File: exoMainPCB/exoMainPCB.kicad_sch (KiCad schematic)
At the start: 1 part

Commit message: centralized schematic sheets into one sheet
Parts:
- added C1, C11, C12, C17, C2, C3, C35, C4: 22 pF, symbol Device:C
- added C10, C27, C30: 0.1 uF, symbol Device:C
- added C13, C14, C8, C9: 100uF, symbol Device:C
- added C15, C16: 10 uF, symbol Device:C
- added C28, C29, C31, C32: 28 pF, symbol Device:C
- added C33, C34, C5, C6: 104, symbol Device:C
- added C7: 100n, symbol Device:C
- added D1, D15, D16, D17, D18, D19, D2, D3: PESD5V0L4UF, Package_TO_SOT_SMD:SOT-886, symbol Power_Protection:PESD5V0L4UF
- added D12, D13, D14: LED, symbol Device:LED
- added J1: Conn_02x06_Odd_Even, symbol Connector_Generic:Conn_02x06_Odd_Even
- added J10, J6: Conn_01x03_Pin, symbol Connector:Conn_01x03_Pin
- added J11, J12, J13, J3: USB_A, symbol Connector:USB_A
- added J2: HDMI_A, symbol Connector:HDMI_A
- added JP1, JP2, JP7, JP8: SolderJumper_2_Open, symbol Jumper:SolderJumper_2_Open
- added Q3, Q4: S8550, Package_TO_SOT_THT:TO-92_Inline, symbol Transistor_BJT:S8550
- added R1, R2: 2.2 kOhm, symbol Device:R_US
- added R10, R8: 2.2k, symbol Device:R_US
- added R11, R4, R5: 10k, symbol Device:R_US
- added R13, R15, R16: R_US, symbol Device:R_US
- added R17, R3, R9: 10 kOhm, symbol Device:R_US
- added R22, R24: 12 kOhm, symbol Device:R_US
- added R23, R25: 17 kOhm, symbol Device:R_US
- added R26, R27: 120, symbol Device:R_US
- added R6, R7: 1k, symbol Device:R_US
- added SW3, SW4: SW_SPDT, symbol Switch:SW_SPDT
- added U1, U2: MCP2515-I/ST, SOP65P640X120-20N, symbol MCP2515-IST:MCP2515-I_ST
- added U12, U13: HX711, Package_SO:SOP-16_3.9x9.9mm_P1.27mm, symbol Analog_ADC:HX711
- added U14: SI8642ED-B-IS, SOIC127P1030X265-16N, symbol SI8642ED-B-IS:Si8642ED-B-IS
- added U15, U16: SN65HVD230D, SOIC127P600X175-8N, symbol SN65HVD230:SN65HVD230D
- added U17, U18: SM24CANB-02HTG, SM24CANB02HTG, symbol SM24CANB:SM24CANB-02HTG
- added U3: BNO085, BNO085:IC_BNO085, symbol BNO085:BNO085
- added U4: SL2.1A, my_lib:SOP-16_L10.0-W3.9-P1.27-LS6.0-BL, symbol SL2.1A:SL2.1A
- added Y1, Y2: 16 MHz, symbol Device:Crystal
- added Y3: 12 MHz, symbol Device:Crystal
- added Y4: 32.768 kHz, symbol Device:Crystal
- added Y7, Y8: 18.432 MHz, symbol Device:Crystal
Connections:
- new net: C10.1, U3.9 (CAP)
- new net: R27.1, SW4.2 (B)
- new net: J10.3 (Pin_3), R27.2, U16.7 (CANH), U18.1
- new net: R5.2, U2.19 (~{RESET})
- new net: R5.1, U2.20 (VDD)
- new net: C3.2, U2.8 (OSC2), Y2.2
- new net: C4.2, U2.9 (OSC1), Y2.1
- new net: D13.2 (A), R15.1
- new net: C15.2, U4.14 (VDD18)
- new net: C29.1, U12.14 (XI), Y7.1
- new net: C28.2, U12.13 (XO), Y7.2
- new net: C32.1, U13.14 (XI), Y8.1
- new net: C31.2, U13.13 (XO), Y8.2
- new net: R26.1, SW3.2 (B)
- new net: J6.3 (Pin_3), R26.2, U15.7 (CANH), U17.1
- new net: C35.2, U4.15 (XOUT), Y3.2
- new net: D14.2 (A), R16.1
- new net: J3.2 (D-), U4.1 (DM4)
- new net: C16.2, U4.13 (VDD33)
- new net: C17.2, U4.16 (XIN), Y3.1
- new net: J3.3 (D+), U4.2 (DP4)
- new net: J11.2 (D-), U4.3 (DM3)
- new net: J11.3 (D+), U4.4 (DP3)
- new net: J12.2 (D-), U4.5 (DM2)
- new net: J12.3 (D+), U4.6 (DP2)
- new net: J13.2 (D-), U4.7 (DM1)
- new net: J13.3 (D+), U4.8 (DP1)
- new net: C34.1, U16.3 (VCC)
- new net: J6.2 (Pin_2), SW3.1 (A), U15.6 (CANL), U17.2
- new net: R7.2, U16.8 (RS)
- new net: J10.2 (Pin_2), SW4.1 (A), U16.6 (CANL), U18.2
- new net: R22.2, R23.1, U12.4 (VFB)
- new net: C5.2, U14.1 (VDD1)
- new net: C6.1, U14.16 (VDD2)
- new net: Q4.2 (B), U13.2 (BASE)
- new net: R4.1, U1.20 (VDD)
- new net: R4.2, U1.19 (~{RESET})
- new net: D12.2 (A), R13.1
- new net: C1.2, U1.8 (OSC2), Y1.2
- new net: C2.2, U1.9 (OSC1), Y1.1
- new net: Q3.2 (B), U12.2 (BASE)
- new net: C27.1, U12.6 (VBG)
- new net: C33.1, U15.3 (VCC)
- new net: C11.1, U3.26 (XOUT32/CLKSEL1), Y4.1
- new net: R6.2, U15.8 (RS)
- new net: R24.2, R25.1, U13.4 (VFB)
- new net: U3.1 (RESV_NC), U3.12 (RESV_NC), U3.13 (RESV_NC), U3.21 (RESV_NC), U3.22 (RESV_NC), U3.23 (RESV_NC), U3.24 (RESV_NC), U3.7 (RESV_NC), U3.8 (RESV_NC)
- new net: C12.1, U3.27 (XIN32), Y4.2
- new net: C30.1, U13.6 (VBG)
- new net +24V: J1.11 (Pin_11), J1.7 (Pin_7), J1.8 (Pin_8)
- new net +3V3: Q3.1 (E), Q4.1 (E), R1.1, R10.2, R11.2, R17.1, R2.1, R3.1, R8.2, R9.2, U12.1 (VSUP), U12.15 (RATE), U12.16 (DVDD), U13.1 (VSUP), U13.15 (RATE), U13.16 (DVDD), U3.28 (VDDIO), U3.3 (VDD)
- new net +5V: C13.1, C14.1, C7.2, C8.1, C9.1, J1.1 (Pin_1), J1.2 (Pin_2), J11.1 (VBUS), J12.1 (VBUS), J13.1 (VBUS), J2.18 (+5V), J3.1 (VBUS), U4.11 (VDD5)
- new net D_{CS0}: U1.18 (~{CS})
- new net D_{CS1}: U2.18 (~{CS})
- new net D_{HDMI0_CEC}: J2.13 (CEC)
- new net D_{HDMI0_CLK_N}: J2.12 (CK-)
- new net D_{HDMI0_CLK_P}: D1.2 (A), D1.5 (A), D3.2 (A), D3.5 (A), J2.10 (CK+)
- new net D_{HDMI0_HOTPLUG}: J2.19 (HPD), R11.1
- new net D_{HDMI0_SCL}: J2.15 (SCL), R10.1
- new net D_{HDMI0_SDA}: J2.16 (SDA), R8.1
- new net D_{HDMI0_TX0_N}: D16.2 (A), D16.5 (A), J2.9 (D0-)
- new net D_{HDMI0_TX0_P}: D18.2 (A), D18.5 (A), J2.7 (D0+)
- new net D_{HDMI0_TX1_N}: D19.2 (A), D19.5 (A), J2.6 (D1-)
- new net D_{HDMI0_TX1_P}: D17.2 (A), D17.5 (A), J2.4 (D1+)
- new net D_{HDMI0_TX2_N}: D15.2 (A), D15.5 (A), J2.3 (D2-)
- new net D_{HDMI0_TX2_P}: D2.2 (A), D2.5 (A), J2.1 (D2+)
- new net D_{INT0}: U1.13 (~{INT})
- new net D_{INT1}: U2.13 (~{INT})
- new net D_{OUT1}: U12.12 (DOUT)
- new net D_{OUT2}: U13.12 (DOUT)
- new net D_{SCK0}: U1.14 (SCK)
- new net D_{SCK1}: U12.11 (PD_SCK), U2.14 (SCK)
- new net D_{SCK2}: U13.11 (PD_SCK)
- new net D_{SI0}: U1.16 (SI)
- new net D_{SI1}: U2.16 (SI)
- new net D_{SO0}: U1.17 (SO)
- new net D_{SO1}: U2.17 (SO)
- new net D_{USB_N}: U4.9 (DM)
- new net D_{USB_P}: U4.10 (DP)
- new net GND: C1.1, C10.2, C11.2, C12.2, C13.2, C14.2, C15.1, C16.1, C17.1, C2.1, C27.2, C28.1, C29.2, C3.1, C30.2, C31.1, C32.2, C35.1, C4.1, C7.1, C8.2, C9.2, D1.1 (K1), D12.1 (K), D13.1 (K), D14.1 (K), D15.1 (K1), D16.1 (K1), D17.1 (K1), D18.1 (K1), D19.1 (K1), D2.1 (K1), D3.1 (K1), J1.3 (Pin_3), J1.4 (Pin_4), J1.5 (Pin_5), J1.6 (Pin_6), J11.4 (GND), J11.5 (Shield), J12.4 (GND), J12.5 (Shield), J13.4 (GND), J13.5 (Shield), J2.17 (GND), J3.4 (GND), J3.5 (Shield), R23.2, R25.2, U1.10 (VSS), U12.5 (AGND), U13.5 (AGND), U14.8 (GND1_2), U2.10 (VSS), U3.17 (SA0/H_MOSI), U3.2 (GND), U3.25 (GNDIO), U3.5 (PS1), U3.6 (PS0/WAKE), U4.12 (GND)
- new net GNDS: C33.2, C34.2, C5.1, C6.2, J10.1 (Pin_1), J6.1 (Pin_1), R6.1, R7.1, U14.15 (GND2_2), U14.2 (GND1_1), U14.9 (GND2_1), U15.2 (GND), U16.2 (GND), U17.3, U18.3
- new net IMU_{BOOT}: R17.2, U3.4 (~{BOOT})
- new net IMU_{HINT}: R3.2, U3.14 (~{H_INT})
- new net IMU_{RST}: U3.11 (~{RST})
- new net P_{IN+}: U12.10 (INB+)
- new net P_{IN-}: U12.9 (INB-)
- new net RXD_0A: JP7.1 (A), U1.2 (RXCAN), U14.5 (A3)
- new net RXD_0B: JP7.2 (B), U14.12 (B3), U15.4 (R)
- new net RXD_1A: JP8.1 (A), U14.6 (A4), U2.2 (RXCAN)
- new net RXD_1B: JP8.2 (B), U14.11 (B4), U16.4 (R)
- new net SCL: R2.2, U3.19 (H_SCL/SCK/RX)
- new net SDA: R1.2, U3.20 (H_SDA/H_MISO/TX)
- new net SG1_{IN+}: U12.8 (INA+)
- new net SG1_{IN-}: U12.7 (INA-)
- new net SG2_{IN+}: U13.8 (INA+)
- new net SG2_{IN-}: U13.7 (INA-)
- new net STATUS_LED_1: R13.2
- new net STATUS_LED_2: R15.2
- new net STATUS_LED_3: R16.2
- new net TXD_0A: JP1.1 (A), U1.1 (TXCAN), U14.3 (A1)
- new net TXD_0B: JP1.2 (B), U14.14 (B1), U15.1 (D)
- new net TXD_1A: JP2.1 (A), U14.4 (A2), U2.1 (TXCAN)
- new net TXD_1B: JP2.2 (B), U14.13 (B2), U16.1 (D)
- new net V_{AVDD1}: Q3.3 (C), R22.1, U12.3 (AVDD)
- new net V_{AVDD2}: Q4.3 (C), R24.1, U13.3 (AVDD)
- new net V_{RP}: J1.10 (Pin_10), J1.9 (Pin_9)
- new net buckStatus: J1.12 (Pin_12), R9.1
- no-connect marks 0 -> 21
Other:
- removed sheet ADC_Amplifiers
- removed sheet Additional_Sensors
- removed sheet Debug
- removed sheet Handheld
- removed sheet IO
- removed sheet Power_Management
- note added: "ADC and Amplifiers"
- note added: "CAN Interface"
- note added: "Debug"
- note added: "Handheld"
- note added: "IMU"
- note added: "Power Management"
- note added: "header for 5V, 5.5A Step-Down Voltage Regulator D36V50F5 check docs at: https://www.pololu.com/product/4091"
- moved on the sheet: Module1A, Module1B

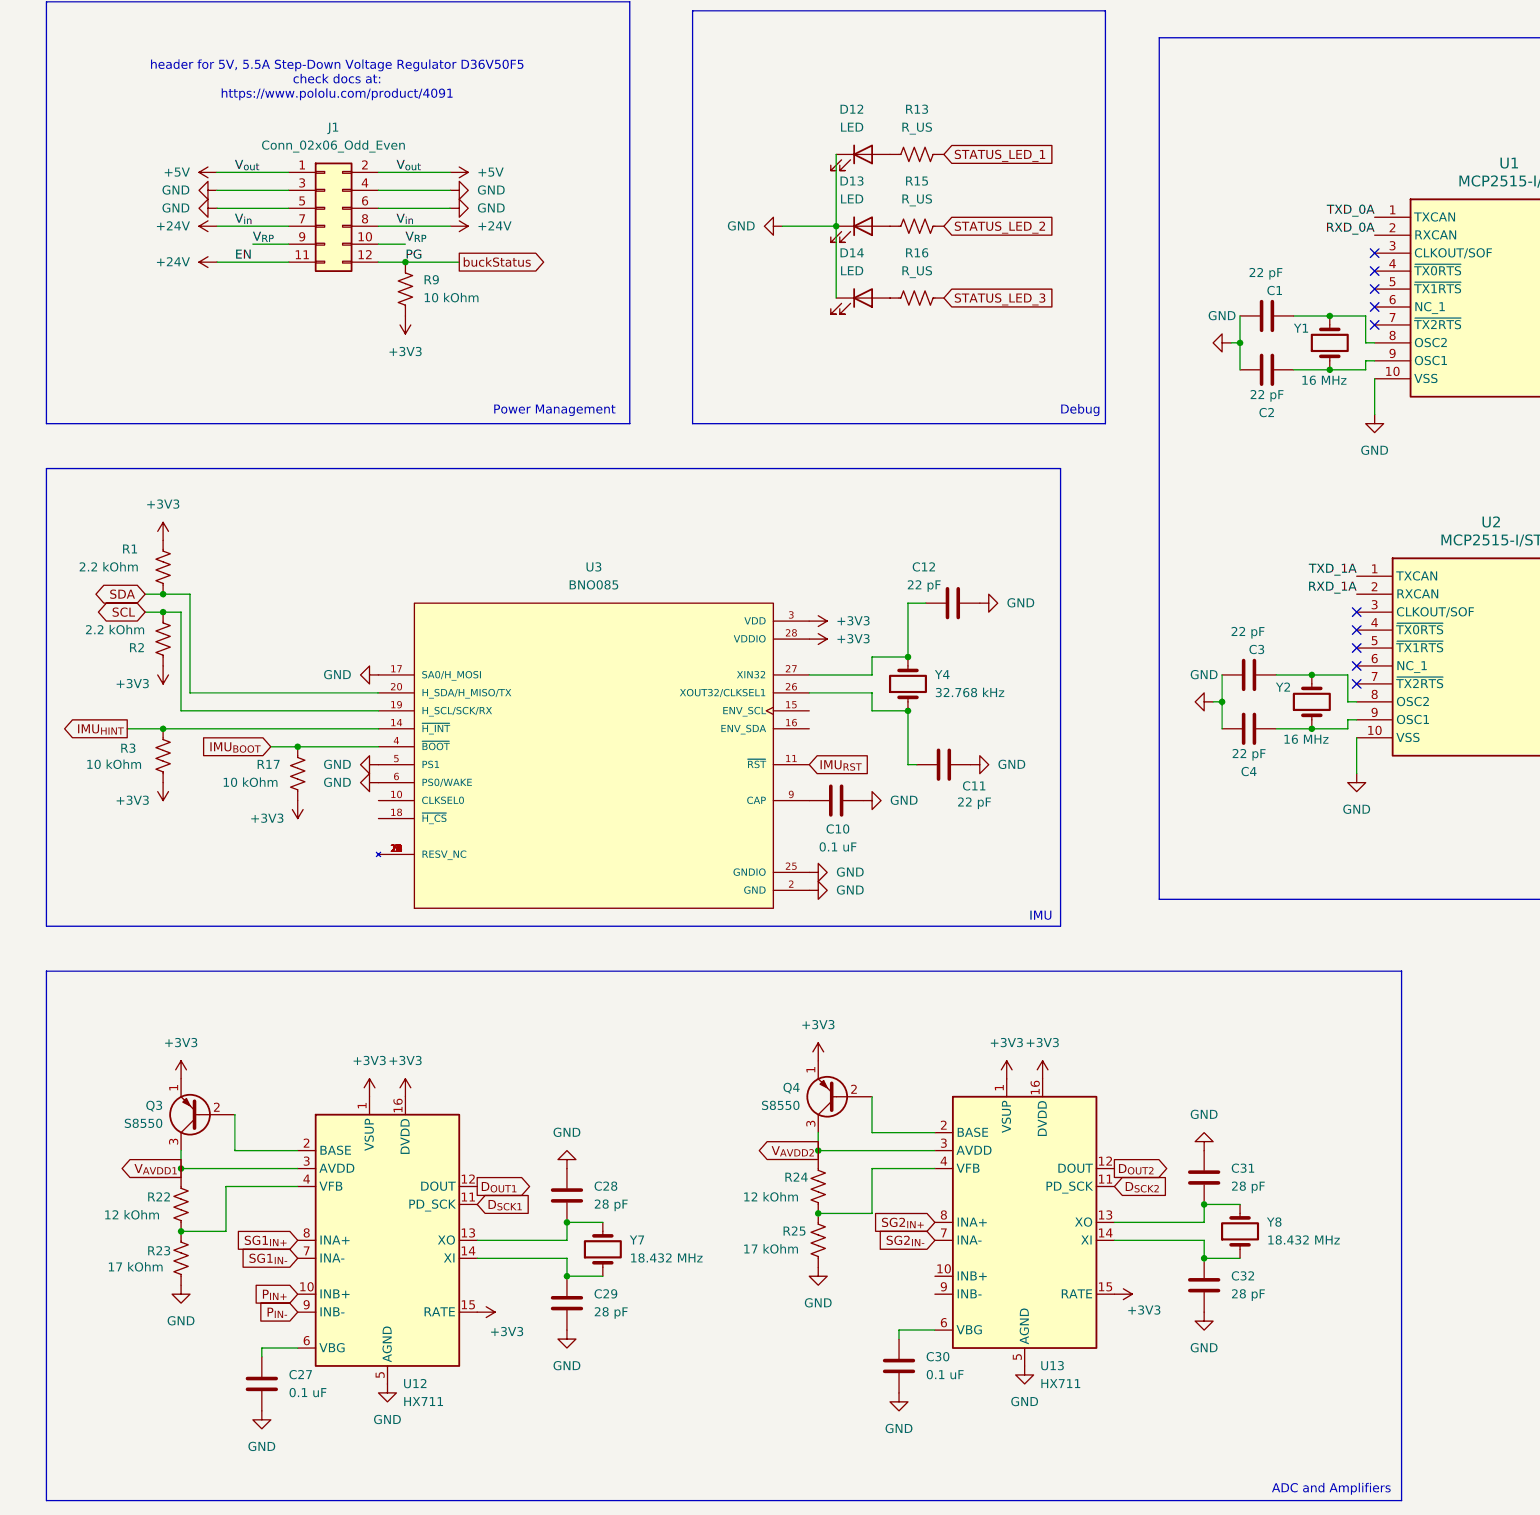
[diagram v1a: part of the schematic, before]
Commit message: replaced hx711 w adc, cleaned up schematics
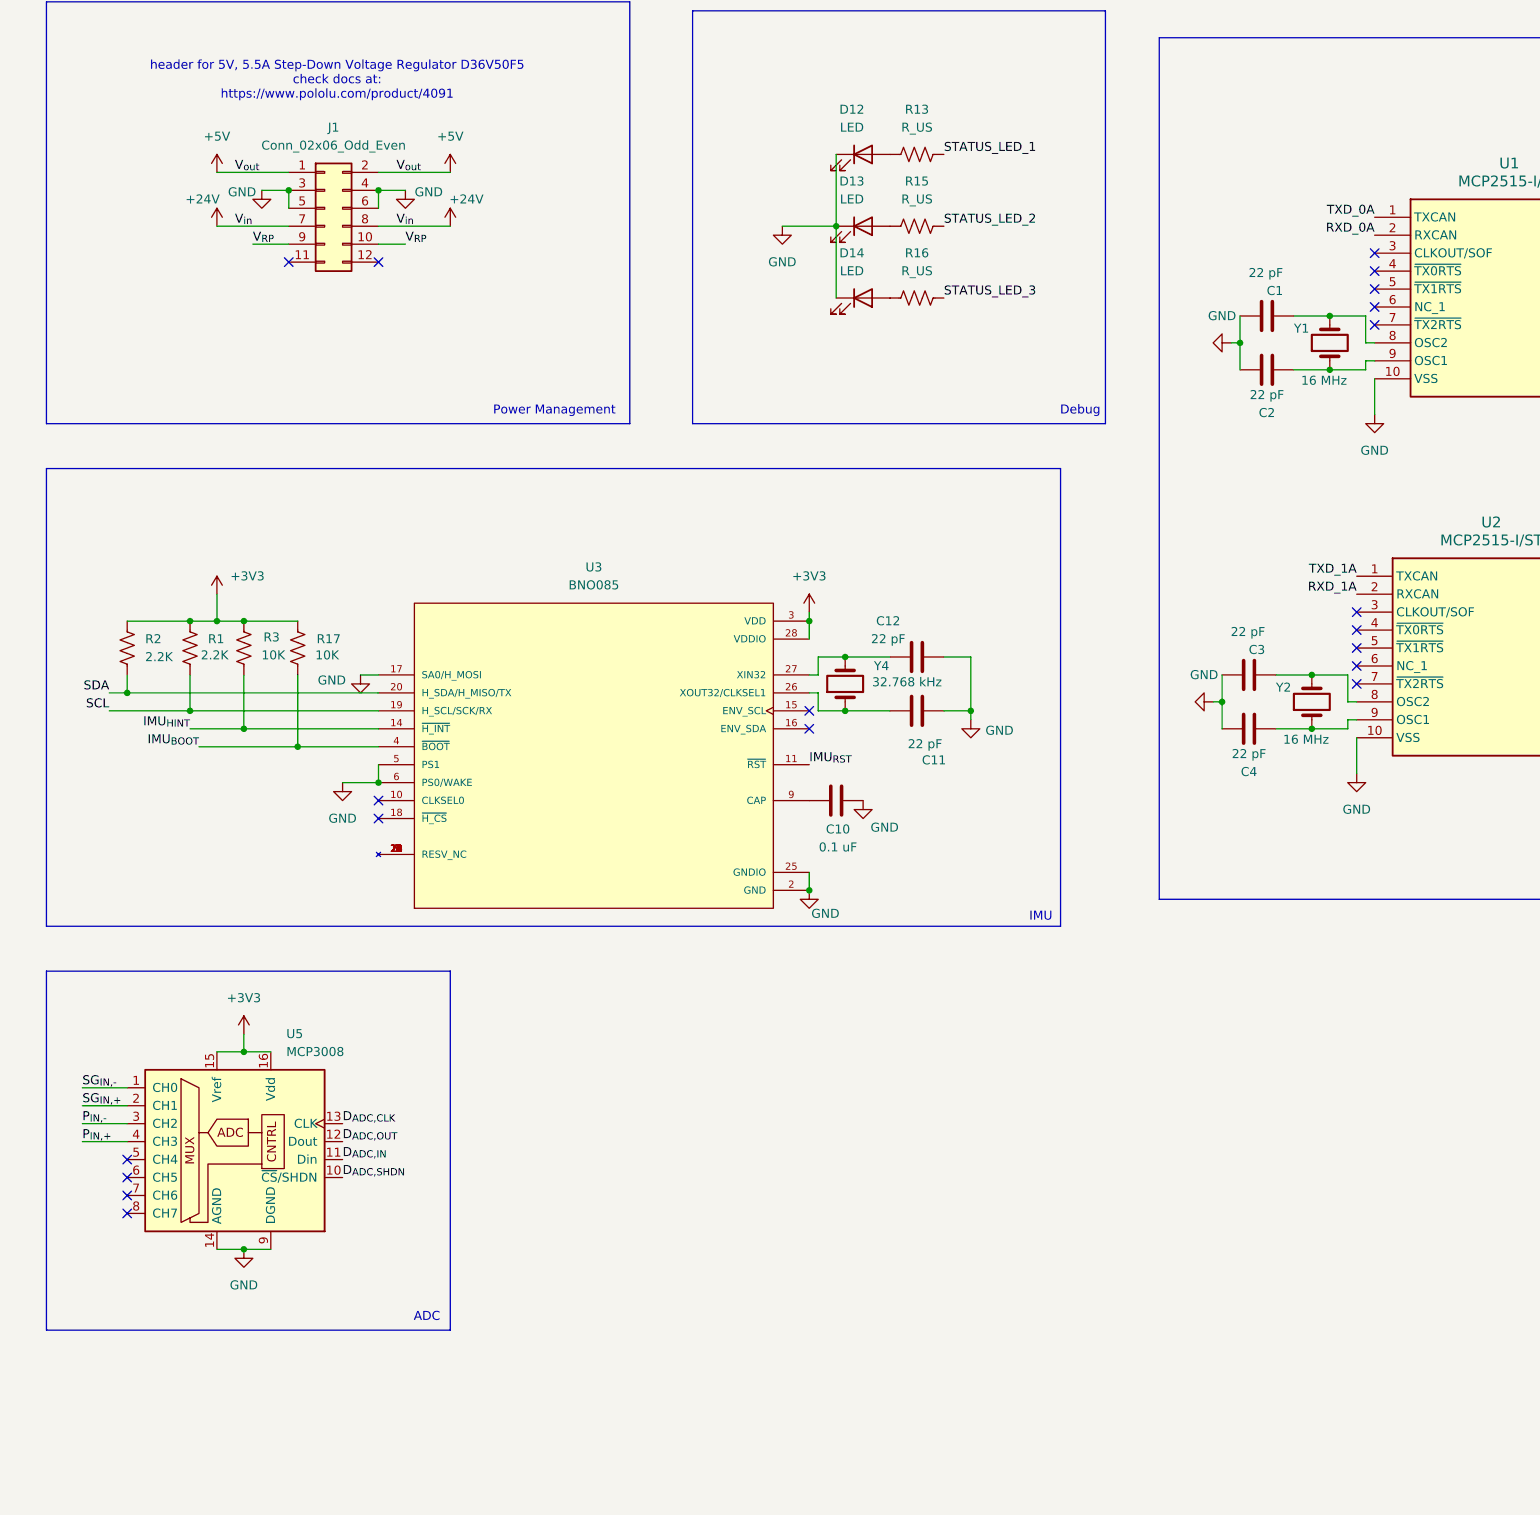
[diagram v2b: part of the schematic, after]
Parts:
- removed C27, C30: 0.1 uF, symbol Device:C
- removed C28, C29, C31, C32: 28 pF, symbol Device:C
- removed Q3, Q4: S8550, Package_TO_SOT_THT:TO-92_Inline, symbol Transistor_BJT:S8550
- removed R22, R24: 12 kOhm, symbol Device:R_US
- removed R23, R25: 17 kOhm, symbol Device:R_US
- removed R9: 10 kOhm, symbol Device:R_US
- removed U12, U13: HX711, Package_SO:SOP-16_3.9x9.9mm_P1.27mm, symbol Analog_ADC:HX711
- removed Y7, Y8: 18.432 MHz, symbol Device:Crystal
- added U5: MCP3008, symbol Analog_ADC:MCP3008
- R1, R2: value 2.2 kOhm -> 2.2K
- R17, R3: value 10 kOhm -> 10K
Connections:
- net +24V: no longer J1.11 (Pin_11)
- net +3V3: now also U5.15 (Vref), U5.16 (Vdd)
- net GND: now also U5.14 (AGND), U5.9 (DGND)
- net SCL: now also R1.2; no longer R2.2
- net SDA: now also R2.2; no longer R1.2
- net buckStatus: no longer names the net of J1.12 (Pin_12)
- new net D_{ADC,CLK}: U5.13 (CLK)
- new net D_{ADC,IN}: U5.11 (Din)
- new net D_{ADC,OUT}: U5.12 (Dout)
- new net D_{ADC,SHDN}: U5.10 (~{CS}/SHDN)
- new net P_{IN,+}: U5.4 (CH3)
- new net P_{IN,-}: U5.3 (CH2)
- new net SG_{IN,+}: U5.2 (CH1)
- new net SG_{IN,-}: U5.1 (CH0)
- no-connect marks 21 -> 31
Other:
- note added: "ADC"
- note removed: "ADC and Amplifiers"
- moved on the sheet: C11, C12, R1, R17, R2, R3, Y4
